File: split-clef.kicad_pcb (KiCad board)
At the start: 2 copper layers, 269 x 84 mm, 42 parts, among them J3 OLED

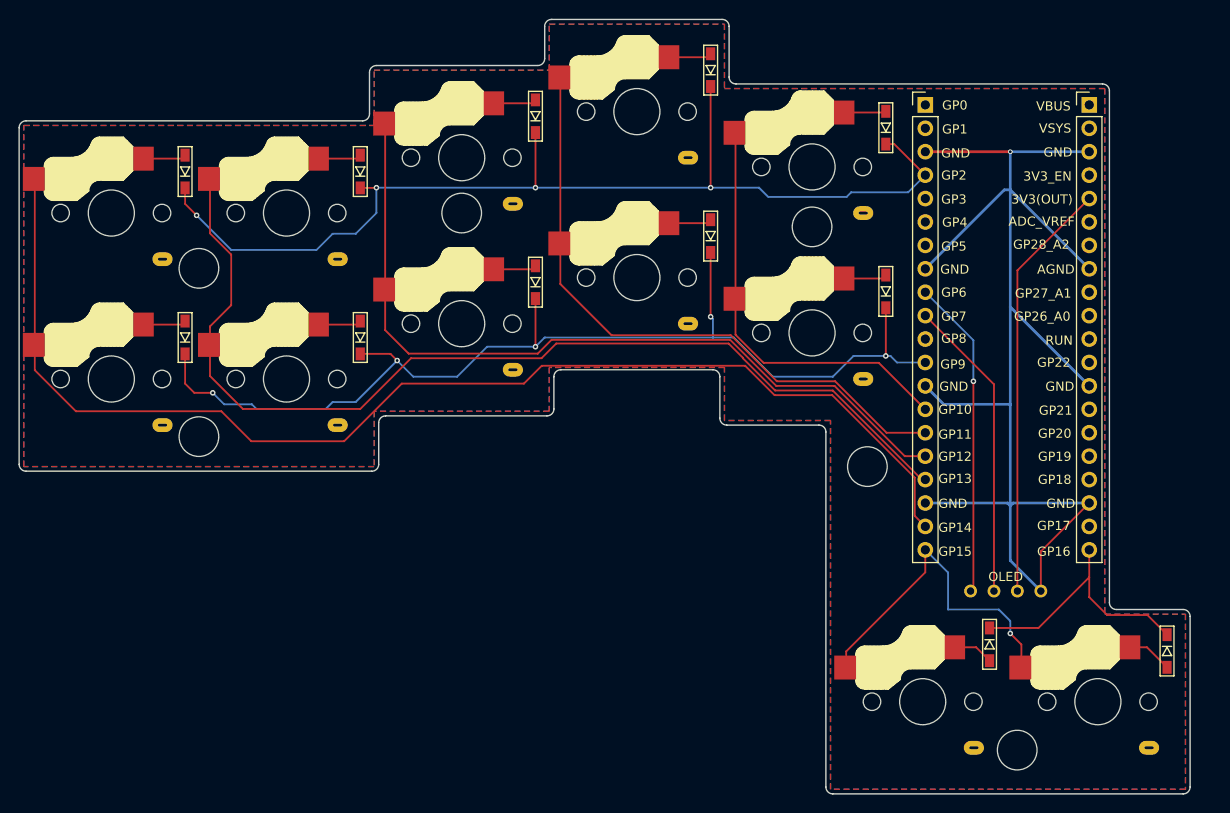
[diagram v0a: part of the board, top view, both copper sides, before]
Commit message: updated to diodeless design and added logo.
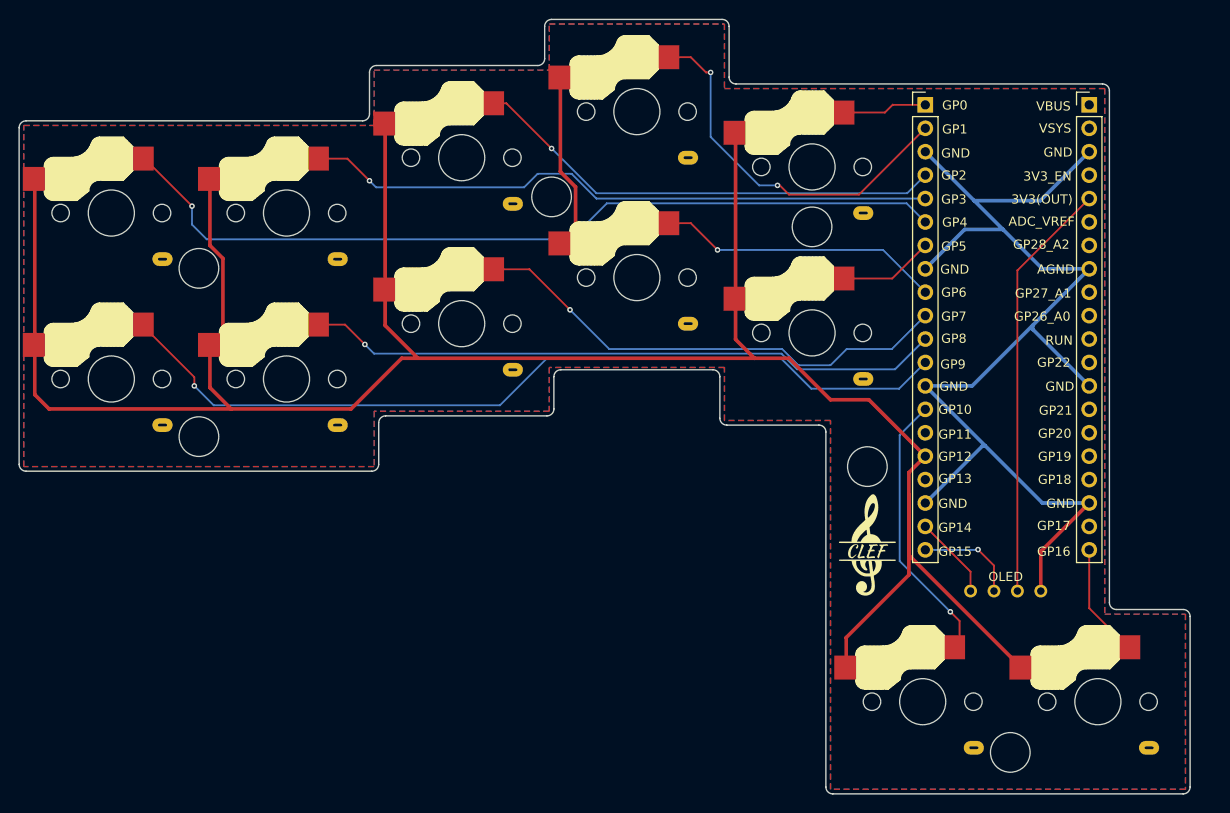
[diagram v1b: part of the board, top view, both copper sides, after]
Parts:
- removed D24 (x12): D, kicad-footprints:D3_SMD_v2
- added G***: LOGO, split-clef:logo, F.Cu at (113.0, 93.0)
- moved Ref** 9.91 mm to (78.8, 55.2)
- moved Ref** 0.79 mm to (128.5, 115.5)
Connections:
- REF** pad 1: (no net) -> LK4
- REF** pad 10: SCL -> LK7
- REF** pad 11: (no net) -> LK6
- REF** pad 12: Row2 -> LK5
- REF** pad 14: Col4 -> LK10
- REF** pad 15: Col3 -> X
- REF** pad 16: Col2 -> left
- REF** pad 19: Col0 -> SDA
- REF** pad 2: (no net) -> LK3
- REF** pad 20: Col6 -> SCL
- REF** pad 21: Row3 -> LK11
- REF** pad 4: Row1 -> LK2
- REF** pad 5: (no net) -> LK1
- REF** pad 6: (no net) -> LK0
- REF** pad 7: (no net) -> LK9
- REF** pad 9: SDA -> LK8
- S1 pad 1: Col1 -> left
- S1 pad 2: D6-Pad2 -> LK6
- S10 pad 1: Col6 -> left
- S10 pad 2: D11-Pad2 -> LK11
- S2 pad 1: Col0 -> left (x2)
- S2 pad 2: D0-Pad2 -> LK0
- S2 pad 2: D5-Pad2 -> LK5
- S2 pad 1: Col1 -> left
- S2 pad 2: D1-Pad2 -> LK1
- S3 pad 1: Col2 -> left
- S3 pad 2: D7-Pad2 -> LK7
- S4 pad 1: Col2 -> left
- S4 pad 2: D2-Pad2 -> LK2
- S5 pad 1: Col3 -> left
- S5 pad 2: D8-Pad2 -> LK8
- S6 pad 1: Col3 -> left
- S6 pad 2: D3-Pad2 -> LK3
- S7 pad 1: Col4 -> left
- S7 pad 2: D9-Pad2 -> LK9
- S8 pad 1: Col4 -> left
- S8 pad 2: D4-Pad2 -> LK4
- S9 pad 1: Col6 -> left
- S9 pad 2: D10-Pad2 -> LK10
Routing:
- net left: track 0.00 -> 276.4 mm
- net Col0: track 133.5 -> 0.00 mm
- net Row2: track 116.4 -> 0.00 mm, vias 5 -> 0
- net Row1: track 114.3 -> 0.00 mm, vias 4 -> 0
- net Col1: track 111.5 -> 0.00 mm
- net LK5: track 0.00 -> 93.8 mm, vias 0 -> 1
- net LK0: track 0.00 -> 92.2 mm, vias 0 -> 1
- net Col2: track 87.9 -> 0.00 mm
- net LK6: track 0.00 -> 69.3 mm, vias 0 -> 1
- net LK1: track 0.00 -> 69.0 mm, vias 0 -> 1
- net Col3: track 68.7 -> 0.00 mm
- net LK7: track 0.00 -> 53.5 mm, vias 0 -> 1
- net LK2: track 0.00 -> 51.8 mm, vias 0 -> 1
- net Col4: track 45.8 -> 0.00 mm
- net LK3: track 0.00 -> 41.2 mm, vias 0 -> 2
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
